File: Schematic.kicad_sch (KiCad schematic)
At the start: 99 parts, among them J1 Screw_Terminal_01x04, J20 T44007, J21 T44007, Q1 HY1707, Q20 BC817, Q21 SUD50P06-15, U1 UC3845, U20 TCMT1108, U21 TL431M, U22 UC3845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

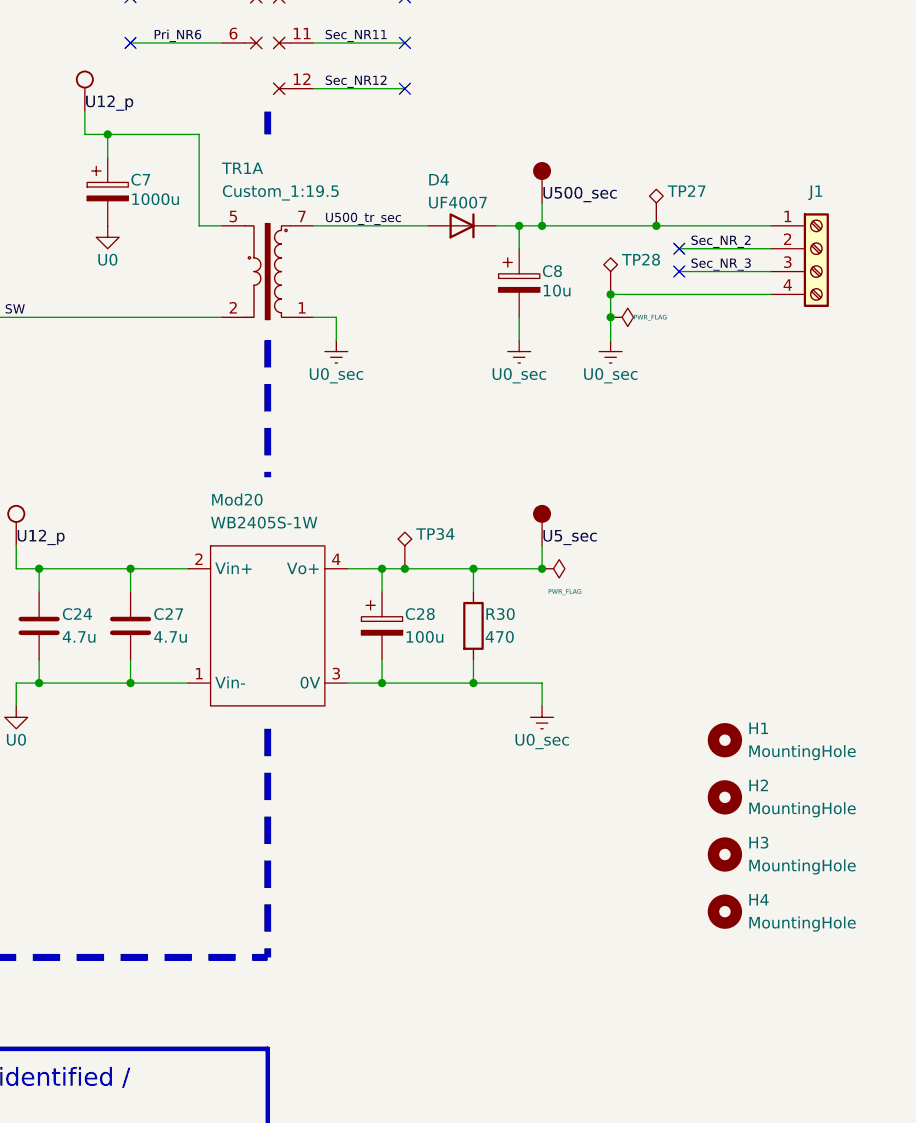
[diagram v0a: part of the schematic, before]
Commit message: Layout rework in progress after checking paper mock up
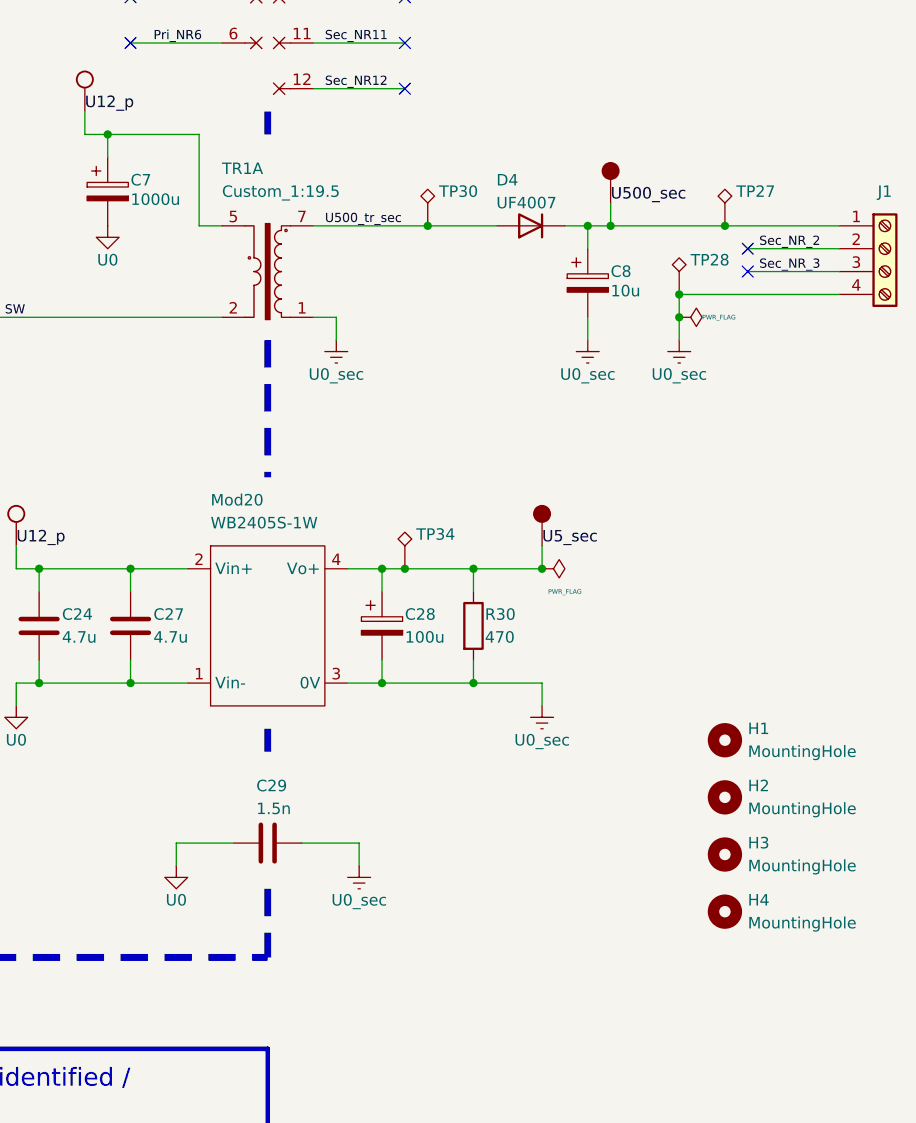
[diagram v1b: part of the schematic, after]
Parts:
- added C29: 1.5n, Capacitor_THT:C_Axial_L3.8mm_D2.6mm_P7.50mm_Horizontal, symbol Device:C
- added TP30: TestPoint_Alt, TestPoint:TestPoint_Loop_D3.50mm_Drill0.9mm_Beaded, symbol Connector:TestPoint_Alt
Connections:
- net U0: now also C29.1
- net U0_sec: now also C29.2
- net U500_tr_sec: now also TP30.1
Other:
- moved on the sheet: C8, D4, J1, TP27, TP28

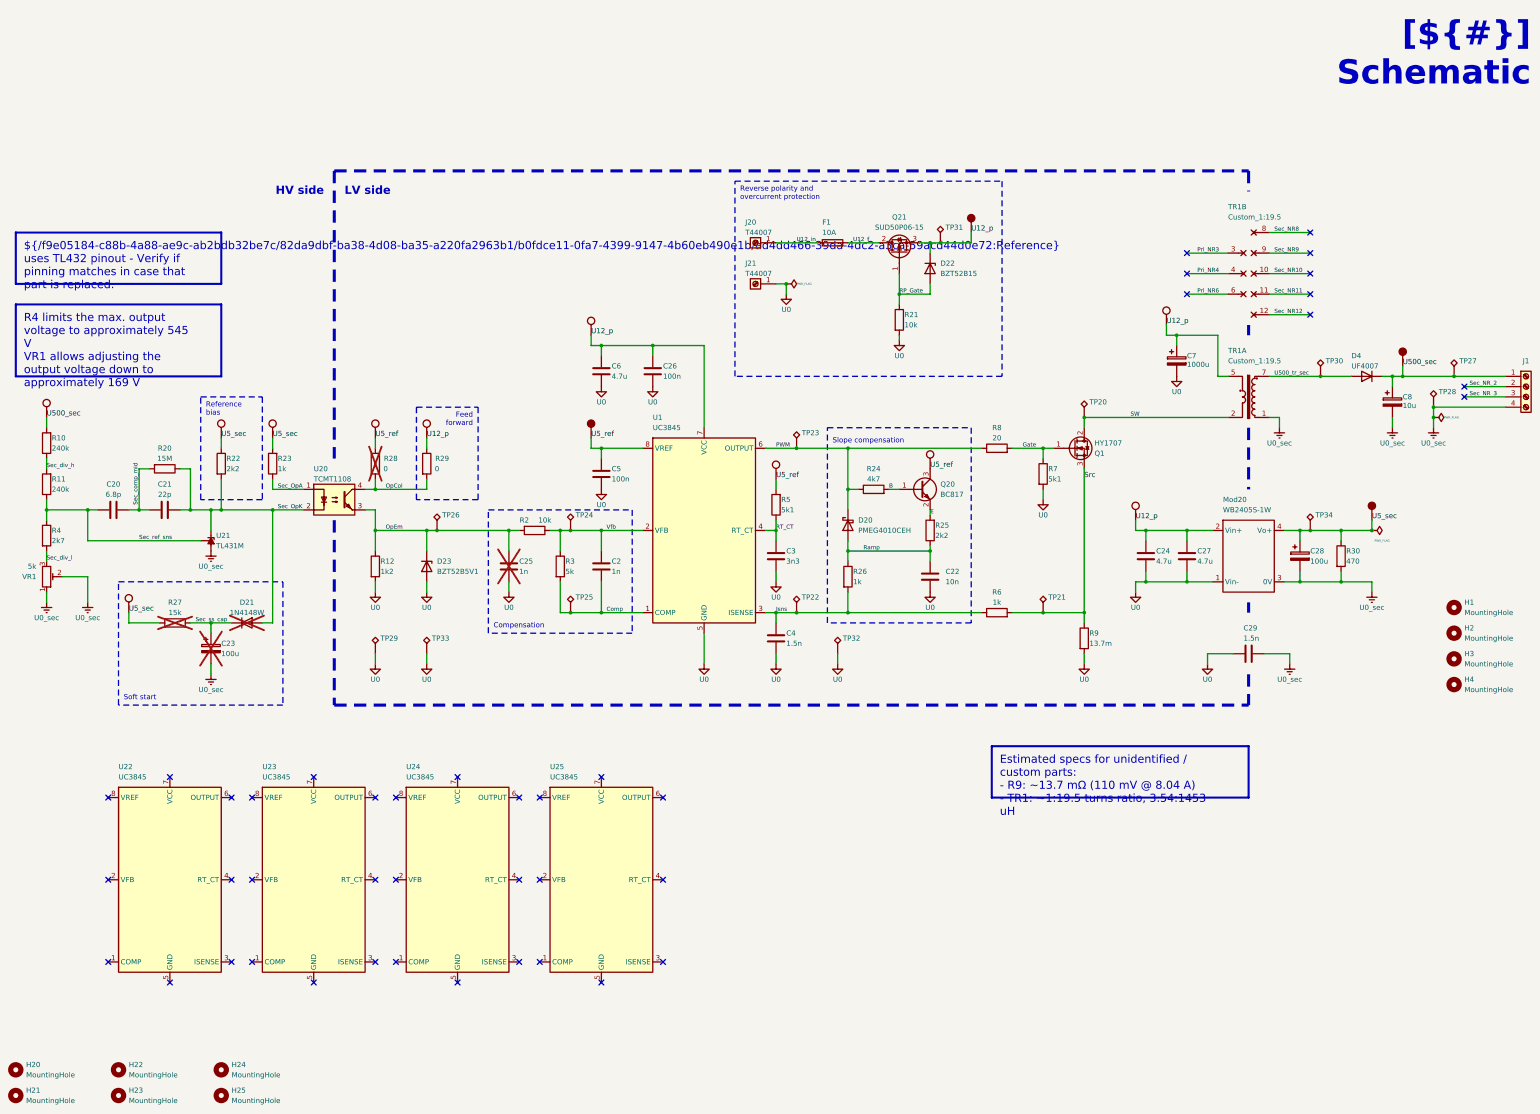
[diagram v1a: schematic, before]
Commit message: Layout ready and checked
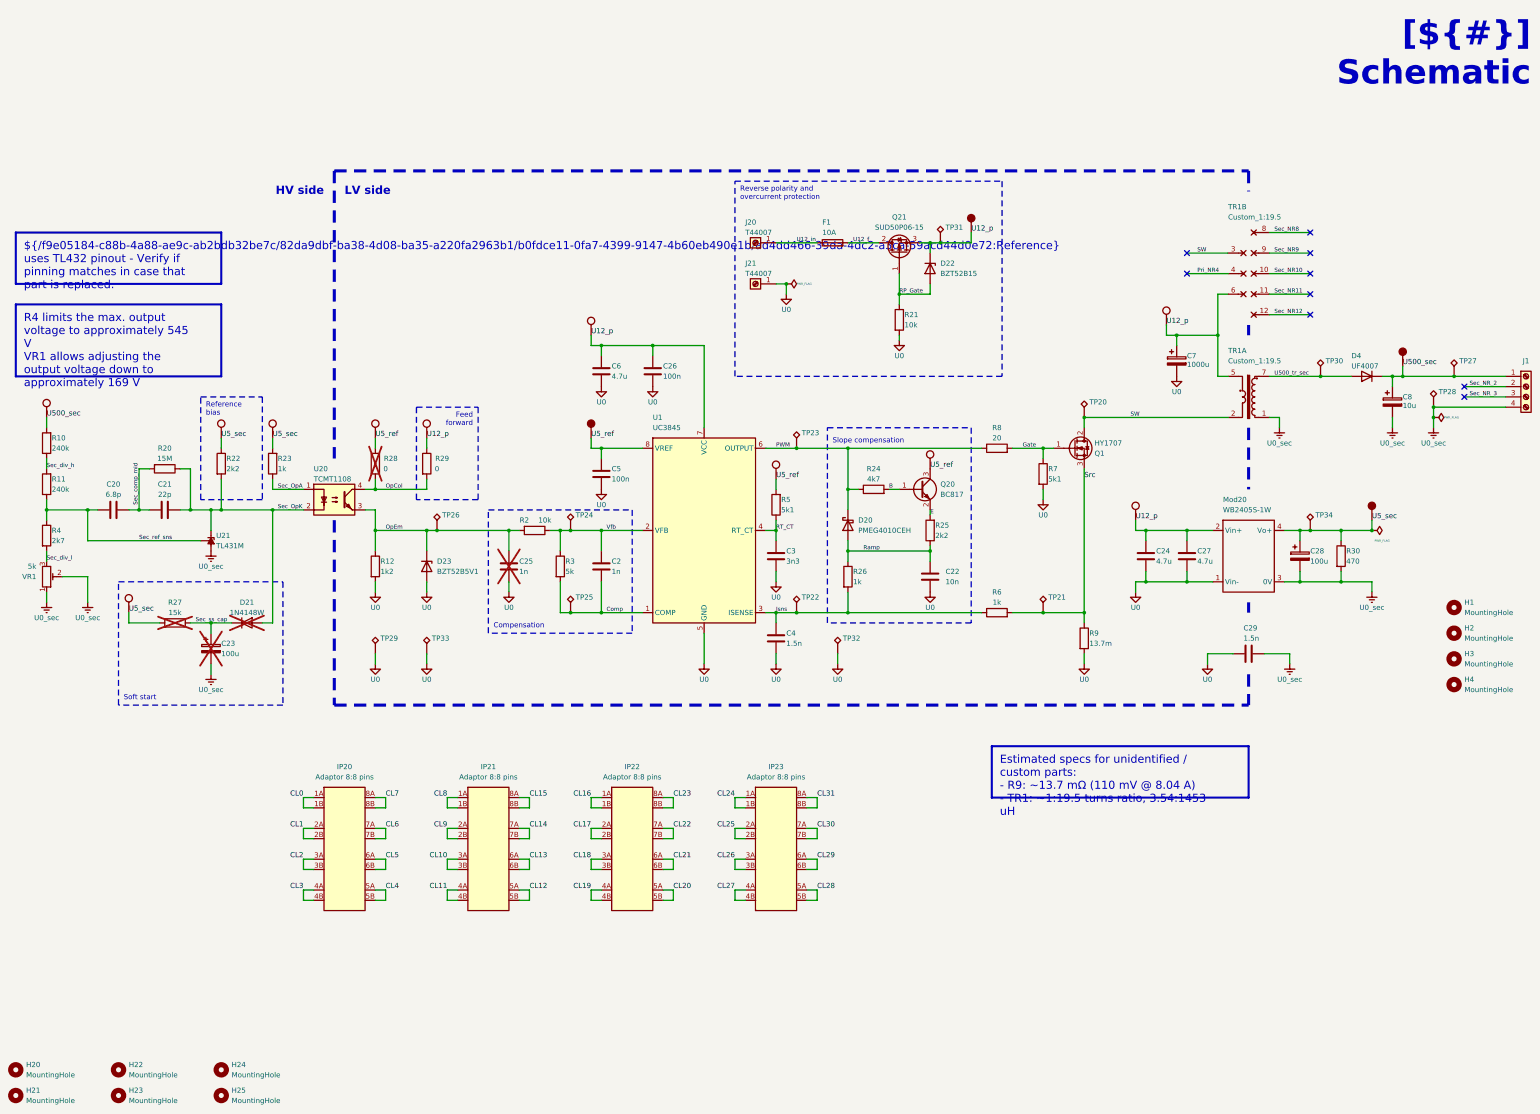
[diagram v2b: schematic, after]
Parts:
- removed U22, U23, U24, U25: UC3845, Personal:Soic-8_to_DIP-8, symbol personal:UC3845
- added IP20, IP21, IP22, IP23: Adaptor 8:8 pins, Personal:Soic-8_to_DIP-8, symbol personal:Adaptor_8_to_8
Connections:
- net Pri_NR3 is gone; now on net SW: TR1.3
- net Pri_NR6 is gone; now on net U12_p: TR1.6
- new net CL0: IP20.1A, IP20.1B
- new net CL1: IP20.2A, IP20.2B
- new net CL10: IP21.3A, IP21.3B
- new net CL11: IP21.4A, IP21.4B
- new net CL12: IP21.5A (5), IP21.5B
- new net CL13: IP21.6A, IP21.6B
- new net CL14: IP21.7A, IP21.7B
- new net CL15: IP21.8A, IP21.8B
- new net CL16: IP22.1A, IP22.1B
- new net CL17: IP22.2A, IP22.2B
- new net CL18: IP22.3A, IP22.3B
- new net CL19: IP22.4A, IP22.4B
- new net CL2: IP20.3A, IP20.3B
- new net CL20: IP22.5A (5), IP22.5B
- new net CL21: IP22.6A, IP22.6B
- new net CL22: IP22.7A, IP22.7B
- new net CL23: IP22.8A, IP22.8B
- new net CL24: IP23.1A, IP23.1B
- new net CL25: IP23.2A, IP23.2B
- new net CL26: IP23.3A, IP23.3B
- new net CL27: IP23.4A, IP23.4B
- new net CL28: IP23.5A (5), IP23.5B
- new net CL29: IP23.6A, IP23.6B
- new net CL3: IP20.4A, IP20.4B
- new net CL30: IP23.7A, IP23.7B
- new net CL31: IP23.8A, IP23.8B
- new net CL4: IP20.5A (5), IP20.5B
- new net CL5: IP20.6A, IP20.6B
- new net CL6: IP20.7A, IP20.7B
- new net CL7: IP20.8A, IP20.8B
- new net CL8: IP21.1A, IP21.1B
- new net CL9: IP21.2A, IP21.2B
- no-connect marks 42 -> 9

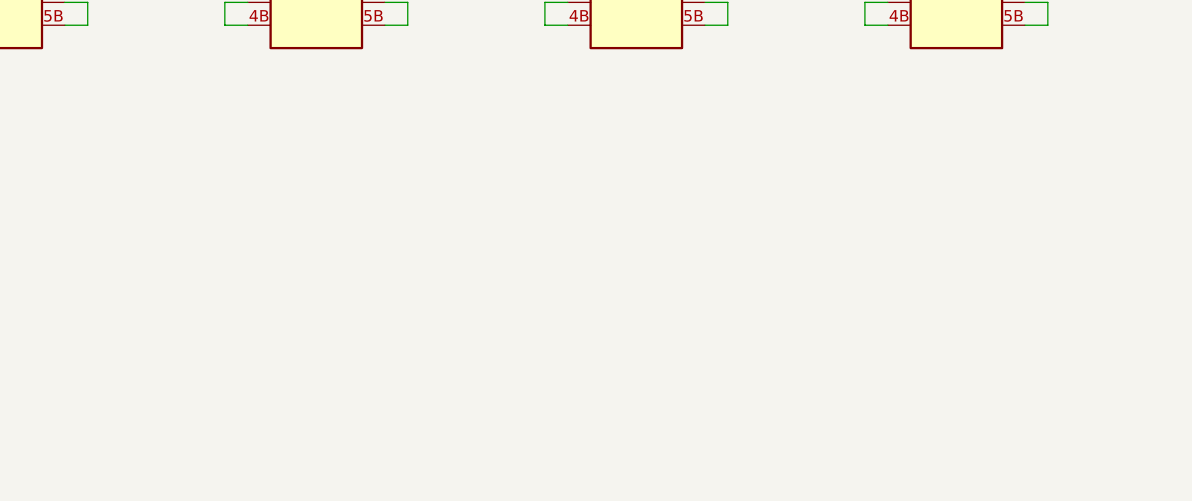
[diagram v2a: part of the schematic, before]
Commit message: Minor changes to resolve potential DFM issues flagged by JLCPCB
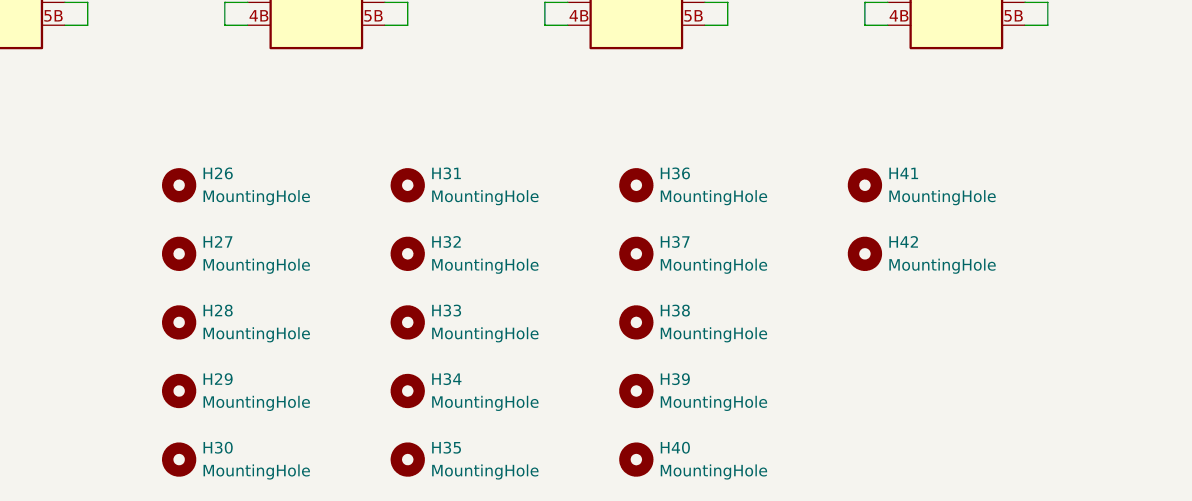
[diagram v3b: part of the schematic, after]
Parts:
- added H26: MountingHole, Personal:Hole_0.3mm, symbol Mechanical:MountingHole
- added H27: MountingHole, Personal:Hole_0.4mm, symbol Mechanical:MountingHole
- added H28: MountingHole, Personal:Hole_0.5mm, symbol Mechanical:MountingHole
- added H29: MountingHole, Personal:Hole_0.6mm, symbol Mechanical:MountingHole
- added H30: MountingHole, Personal:Hole_0.7mm, symbol Mechanical:MountingHole
- added H31: MountingHole, Personal:Hole_0.8mm, symbol Mechanical:MountingHole
- added H32: MountingHole, Personal:Hole_0.9mm, symbol Mechanical:MountingHole
- added H33: MountingHole, Personal:Hole_1.0mm, symbol Mechanical:MountingHole
- added H34: MountingHole, Personal:Hole_1.2mm, symbol Mechanical:MountingHole
- added H35: MountingHole, Personal:Hole_1.4mm, symbol Mechanical:MountingHole
- added H36: MountingHole, Personal:Hole_1.6mm, symbol Mechanical:MountingHole
- added H37: MountingHole, Personal:Hole_1.8mm, symbol Mechanical:MountingHole
- added H38: MountingHole, Personal:Hole_2.0mm, symbol Mechanical:MountingHole
- added H39: MountingHole, Personal:Hole_2.5mm, symbol Mechanical:MountingHole
- added H40: MountingHole, Personal:Hole_3.0mm, symbol Mechanical:MountingHole
- added H41: MountingHole, Personal:Hole_3.5mm, symbol Mechanical:MountingHole
- added H42: MountingHole, Personal:Hole_4.0mm, symbol Mechanical:MountingHole
